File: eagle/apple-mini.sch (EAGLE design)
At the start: 30 parts, among them J1 USBMICRO, J2 RBM22DRTN, J3 JTAG, U1 FT240XS, U2 SN74LVC2G17DBV, U3 TPS2082D, U4 XC9572XL-10VQ64

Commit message: Add MPU and PIA to schematic
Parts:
- added C12, C13, C14, C15: 0.1uF, rcl:C-USC0805
- added R10, R11, R12: 100k, rcl:R-US_R0805
- added U5: 6821, apple-mini:6821
- added U6: 62256, apple-mini:62256
- added U7: 28C64, apple-mini:28C64
- added U8: XC9572XL-10VQ64, apple-mini:XC9572XL-10VQ64
- J2: value RBM22DRTN -> JTAG; device apple-mini:RBM22DRTN -> apple-mini:JTAG
- J3: value JTAG -> RBM22DRTN; device apple-mini:JTAG -> apple-mini:RBM22DRTN
- U2: value SN74LVC2G17DBV -> 74LVC2G17DBV; device apple-mini:SN74LVC2G17DBV -> apple-mini:74LVC2G17DBV
- U4: value XC9572XL-10VQ64 -> 6502; device apple-mini:XC9572XL-10VQ64 -> apple-mini:6502
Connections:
- net 3V3: now also C12.1, C13.1, C14.1, C15.1, J2.VREF, R10.2, R11.2, R12.2, U4P.VCC, U5G$1.CS1, U5G$1.PA7, U5P.VCC, U6P.VCC, U7P.VCC, U8PA.VCC, U8PB.VCC, U8PC.VCC, U8PD.VCC; no longer J3.VREF, U4PA.VCC, U4PB.VCC, U4PC.VCC, U4PD.VCC
- net 5V: now also J3.22; no longer J2.22
- net A0: now also J3.W, U4G$1.A0, U5G$1.RS0, U6G$1.A0, U7G$1.A0, U8G$1.P57; no longer J2.W, U4G$1.P57
- net A1: now also J3.19, U4G$1.A1, U5G$1.RS1, U6G$1.A1, U7G$1.A1, U8G$1.P59; no longer J2.19, U4G$1.P59
- net A10: now also J3.R, U4G$1.A10, U6G$1.A10, U7G$1.A10; no longer J2.R
- net A11: now also J3.14, U4G$1.A11, U6G$1.A11, U7G$1.A11; no longer J2.14
- net A12: now also J3.P, U4G$1.A12, U6G$1.A12, U7G$1.A12; no longer J2.P
- net A13: now also J3.13, U4G$1.A13, U6G$1.A13; no longer J2.13
- net A14: now also J3.N, U4G$1.A14, U6G$1.A14; no longer J2.N
- net A15: now also J3.12, U4G$1.A15; no longer J2.12
- net A2: now also J3.V, U4G$1.A2, U6G$1.A2, U7G$1.A2, U8G$1.P50; no longer J2.V, U4G$1.P50
- net A3: now also J3.18, U4G$1.A3, U6G$1.A3, U7G$1.A3, U8G$1.P2/GTS2; no longer J2.18, U4G$1.P2/GTS2
- net A4: now also J3.U, U4G$1.A4, U5G$1.CS0, U6G$1.A4, U7G$1.A4; no longer J2.U
- net A5: now also J3.17, U4G$1.A5, U6G$1.A5, U7G$1.A5; no longer J2.17
- net A6: now also J3.T, U4G$1.A6, U6G$1.A6, U7G$1.A6; no longer J2.T
- net A7: now also J3.16, U4G$1.A7, U6G$1.A7, U7G$1.A7; no longer J2.16
- net A8: now also J3.S, U4G$1.A8, U6G$1.A8, U7G$1.A8; no longer J2.S
- net A9: now also J3.15, U4G$1.A9, U6G$1.A9, U7G$1.A9; no longer J2.15
- net CA1: now also U5G$1.CA1, U8G$1.P52; no longer U4G$1.P52
- net CA2: now also U5G$1.CA2, U8G$1.P56; no longer U4G$1.P56
- net CB1: now also U5G$1.CB1, U8G$1.P19; no longer U4G$1.P19
- net CB2: now also U5G$1.CB2, U8G$1.P40; no longer U4G$1.P40
- net CLEAR: now also U8G$1.P31; no longer U4G$1.P31
- net CLK12MHZ: now also U8G$1.P16/GCK2; no longer U4G$1.P16/GCK2
- net D0: now also J3.9, U4G$1.D0, U5G$1.D0, U6G$1.D0, U7G$1.D0; no longer J2.9
- net D1: now also J3.J, U4G$1.D1, U5G$1.D1, U6G$1.D1, U7G$1.D1; no longer J2.J
- net D2: now also J3.8, U4G$1.D2, U5G$1.D2, U6G$1.D2, U7G$1.D2; no longer J2.8
- net D3: now also J3.H, U4G$1.D3, U5G$1.D3, U6G$1.D3, U7G$1.D3; no longer J2.H
- net D4: now also J3.7, U4G$1.D4, U5G$1.D4, U6G$1.D4, U7G$1.D4; no longer J2.7
- net D5: now also J3.F, U4G$1.D5, U5G$1.D5, U6G$1.D5, U7G$1.D5; no longer J2.F
- net D6: now also J3.6, U4G$1.D6, U5G$1.D6, U6G$1.D6, U7G$1.D6; no longer J2.6
- net D7: now also J3.E, U4G$1.D7, U5G$1.D7, U6G$1.D7, U7G$1.D7; no longer J2.E
- net DA: now also U5G$1.PB7, U8G$1.P20; no longer U4G$1.P20
- net FIFO_DATA0: now also U8G$1.P43; no longer U4G$1.P43
- net FIFO_DATA1: now also U8G$1.P44; no longer U4G$1.P44
- net FIFO_DATA2: now also U8G$1.P49; no longer U4G$1.P49
- net FIFO_DATA3: now also U8G$1.P51; no longer U4G$1.P51
- net FIFO_DATA4: now also U8G$1.P8; no longer U4G$1.P8
- net FIFO_DATA5: now also U8G$1.P9; no longer U4G$1.P9
- net FIFO_DATA6: now also U8G$1.P10; no longer U4G$1.P10
- net FIFO_DATA7: now also U8G$1.P39; no longer U4G$1.P39
- net FIFO_RD: now also U8G$1.P22; no longer U4G$1.P22
- net FIFO_RXF: now also U8G$1.P48; no longer U4G$1.P48
- net FIFO_TXE: now also U8G$1.P45; no longer U4G$1.P45
- net FIFO_WR: now also U8G$1.P18; no longer U4G$1.P18
- net GND: now also C12.2, C13.2, C14.2, C15.2, J2.GND, J3.20, J3.X, U4G$1.!SO, U4P.GND, U5P.GND, U6P.GND, U7P.GND, U8G$1.P15/GCK1, U8G$1.P17/GCK3, U8G$1.P23, U8G$1.P25, U8G$1.P32, U8G$1.P36, U8PA.GND, U8PB.GND, U8PC.GND, U8PD.GND; no longer J2.20, J2.X, J3.GND, U4G$1.P15/GCK1, U4G$1.P17/GCK3, U4G$1.P23, U4G$1.P25, U4G$1.P32, U4G$1.P36, U4PA.GND, U4PB.GND, U4PC.GND, U4PD.GND
- net IRQ: now also J3.4, R11.1, U4G$1.!IRQ; no longer J2.4
- net NMI: now also J3.3, R12.1, U4G$1.!NMI; no longer J2.3
- net PA0: now also U5G$1.PA0, U8G$1.P6; no longer U4G$1.P6
- net PA1: now also U5G$1.PA1, U8G$1.P60; no longer U4G$1.P60
- net PA2: now also U5G$1.PA2, U8G$1.P58; no longer U4G$1.P58
- net PA3: now also U5G$1.PA3, U8G$1.P62; no longer U4G$1.P62
- net PA4: now also U5G$1.PA4, U8G$1.P63; no longer U4G$1.P63
- net PA5: now also U5G$1.PA5, U8G$1.GSR/P64; no longer U4G$1.GSR/P64
- net PA6: now also U5G$1.PA6, U8G$1.P4; no longer U4G$1.P4
- net PB0: now also U5G$1.PB0, U8G$1.P61; no longer U4G$1.P61
- net PB1: now also U5G$1.PB1, U8G$1.P5/GTS1; no longer U4G$1.P5/GTS1
- net PB2: now also U5G$1.PB2, U8G$1.P46; no longer U4G$1.P46
- net PB3: now also U5G$1.PB3, U8G$1.P7; no longer U4G$1.P7
- net PB4: now also U5G$1.PB4, U8G$1.P11; no longer U4G$1.P11
- net PB5: now also U5G$1.PB5, U8G$1.P13; no longer U4G$1.P13
- net PB6: now also U5G$1.PB6, U8G$1.P12; no longer U4G$1.P12
- net PHI0: now also J3.M, U4G$1.PHI0, U8G$1.P24; no longer J2.M, U4G$1.P24
- net PHI1: now also J3.D, U4G$1.PHI1; no longer J2.D
- net PHI2: now also J3.A, U4G$1.PHI2, U5G$1.E, U8G$1.P47; no longer J2.A, U4G$1.P47
- net R: now also J3.L, U8G$1.P27; no longer J2.L, U4G$1.P27
- net RDY: now also J3.5, R10.1, U4G$1.RDY; no longer J2.5
- net RESET: now also J3.2, U4G$1.!RES, U5G$1.!RESET, U8G$1.P1; no longer J2.2, U4G$1.P1
- net RW: now also J3.K, U4G$1.R/!W, U5G$1.R/!W, U6G$1.!WE, U7G$1.!WE; no longer J2.K
- net S: now also J3.11, U8G$1.P33; no longer J2.11, U4G$1.P33
- net SYNC: now also J3.B, U4G$1.SYNC; no longer J2.B
- net T: now also J3.21, U8G$1.P35; no longer J2.21, U4G$1.P35
- net TCK: now also J2.TCK, U8G$1.TCK; no longer J3.TCK, U4G$1.TCK
- net TDI: now also J2.TDI, U8G$1.TDI; no longer J3.TDI, U4G$1.TDI
- net TDO: now also J2.TDO, U8G$1.TDO; no longer J3.TDO, U4G$1.TDO
- net TMS: now also J2.TMS, U8G$1.TMS; no longer J3.TMS, U4G$1.TMS
- net X: now also U6G$1.!CE, U6G$1.!OE, U8G$1.P34; no longer U4G$1.P34
- net Y: now also U7G$1.!CE, U7G$1.!OE, U8G$1.P42; no longer U4G$1.P42
- net Z: now also U5G$1.!CS2, U8G$1.P38; no longer U4G$1.P38
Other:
- note added: "MEMORY MAP X 0000 7FFF RAM T A000 AFFF S B000 BFFF R C000 CFFF Z D000 DFFF PIA Y E000 FFFF EEPROM"

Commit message: Finalize schematic; initial board placement
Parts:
- C1, C10, C11, C12, C13, C14, C15, C2, C3, C6, C7, C8, C9: device rcl:C-USC0805 -> apple-mini:C0603
- C4, C5: value 0.22uF -> 2.2uF; device rcl:C-USC0805 -> apple-mini:C0603
- D1: value (none) -> CHIPLED; device led:LEDCHIP-LED0805 -> apple-mini:CHIPLED
- R1, R2: device rcl:R-US_R0805 -> apple-mini:R0402
- R10, R11, R12, R4, R5: value 100k -> 10k; device rcl:R-US_R0805 -> apple-mini:R0603
- R3, R9: value 100k -> 4.7k; device rcl:R-US_R0805 -> apple-mini:R0603
- R6, R7, R8: device rcl:R-US_R0805 -> apple-mini:R0603
- U2: value 74LVC2G17DBV -> SN74LVC2G17DBV; device apple-mini:74LVC2G17DBV -> apple-mini:SN74LVC2G17DBV
- U4: value 6502 -> MCS6502; device apple-mini:6502 -> apple-mini:MCS6502
- U5: value 6821 -> MC6821; device apple-mini:6821 -> apple-mini:MC6821
- U6: value 62256 -> AS6C62256A; device apple-mini:62256 -> apple-mini:AS6C62256A
- U7: value 28C64 -> AT28C64B; device apple-mini:28C64 -> apple-mini:AT28C64B
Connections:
- net 3V3: no longer C10.1, C11.1, C2.1, C8.1, C9.1, R10.2, R11.2, R12.2, R4.2, R5.2, U2P.VCC, U4P.VCC, U5G$1.CS1, U5G$1.PA7, U5P.VCC, U6P.VCC, U7P.VCC
- net 5V: now also C10.1, C11.1, C2.1, C8.1, C9.1, D1.2, R10.2, R11.2, R12.2, R4.2, R5.2, U2P.VCC, U4P.VCC, U5G$1.CS1, U5G$1.PA7, U5P.VCC, U6P.VCC, U7P.VCC; no longer D1.A
- net CLEAR: now also U2B.Y; no longer U2A.Y
- net GND: now also RESET.3; no longer RESET.4
- net N$1: now also D1.1; no longer D1.C
- net N$2: now also R7.1; no longer R6.1
- net N$3: now also R6.1, RESET.1; no longer R7.1, RESET.2
- net RESET: now also U2A.Y, U4G$1.!RESET; no longer U2B.Y, U4G$1.!RES
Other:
- note added: "KEYBOARD"
- note added: "TERMINAL"
- moved on the sheet: C1, C10, C11, C12, C13, C14, C15, C2, C4, C5, C8, C9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

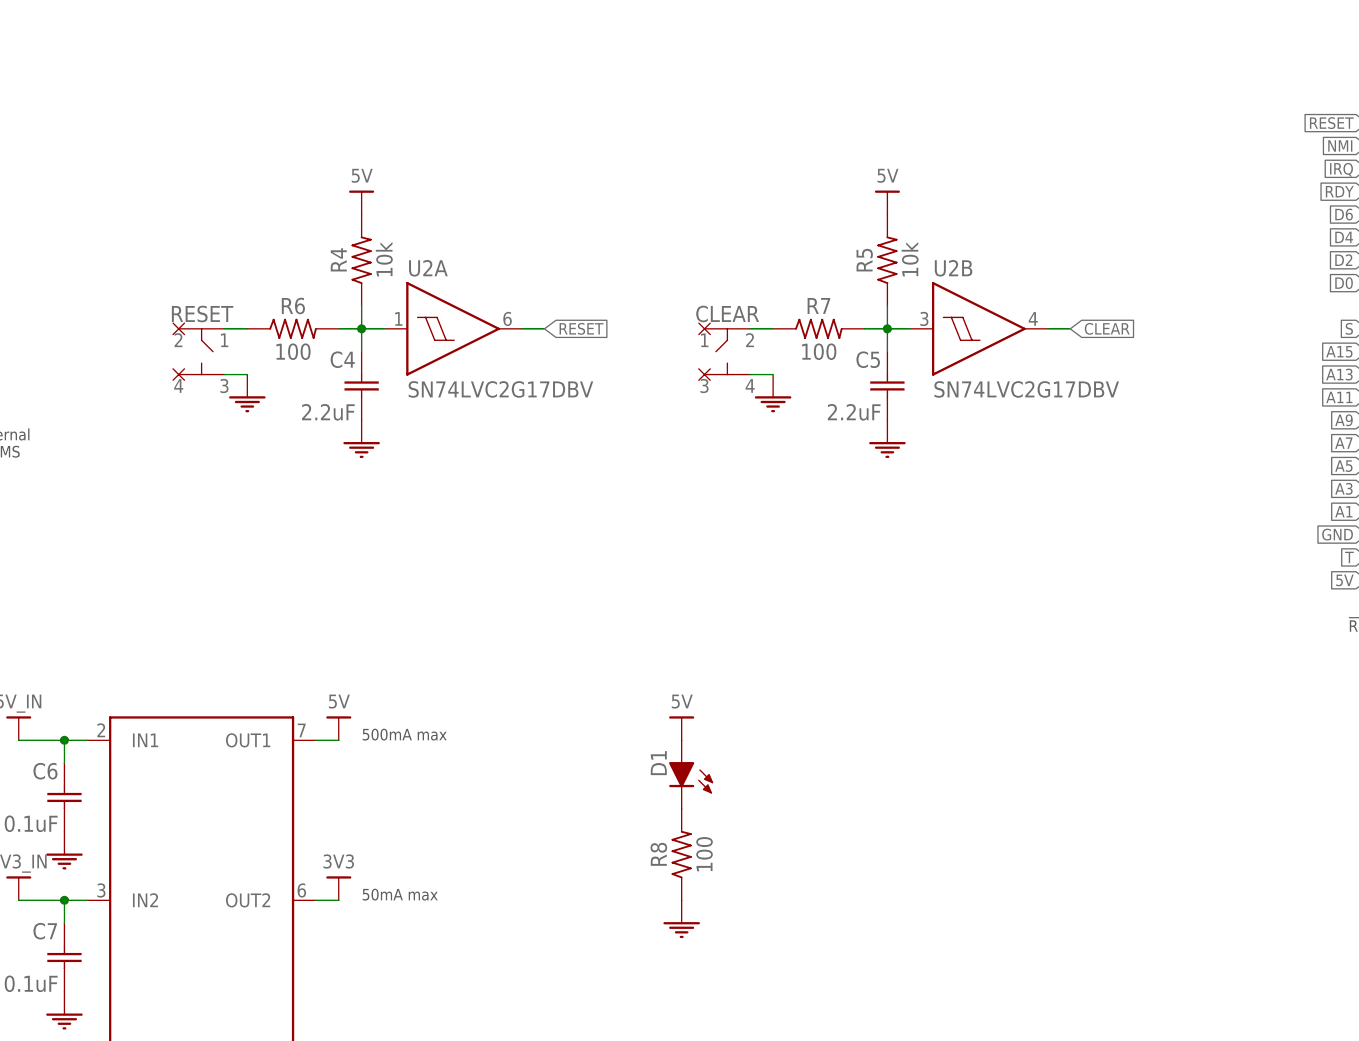
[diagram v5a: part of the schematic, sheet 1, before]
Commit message: Add DRC rules and logo bitmap to board layout
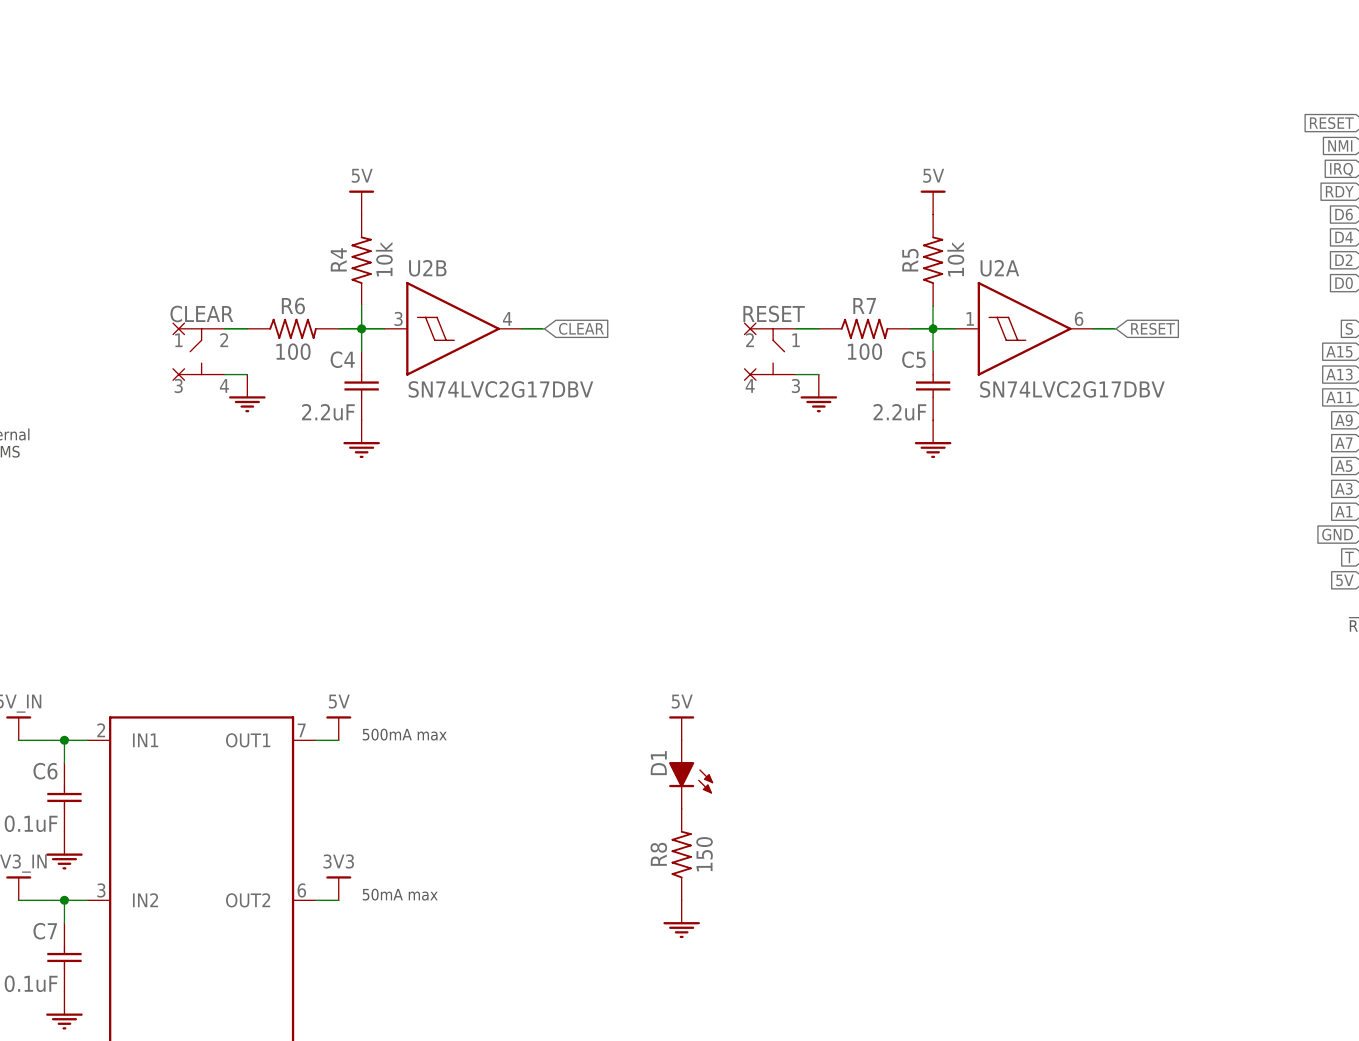
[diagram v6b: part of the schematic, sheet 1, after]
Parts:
- R8: value 100 -> 150
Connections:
- net N$2: now also R6.1; no longer R7.1
- net N$3: now also R7.1; no longer R6.1
- net N$4: now also C4.1, R4.1, R6.2; no longer C5.1, R5.1, R7.2
- net N$5: now also C5.1, R5.1, R7.2; no longer C4.1, R4.1, R6.2
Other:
- moved on the sheet: C5, CLEAR, R5, R7, RESET, U2A, U2B

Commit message: Generate BOM
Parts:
- C1, C10, C11, C12, C13, C14, C15, C2, C3, C6, C7, C8, C9: COMMENTS (none) -> 16V 10% X7R MLCC; MFR (none) -> Kemet; MFR_PARTNO (none) -> C0603C104K4RACTU; VENDOR (none) -> Digi-Key; VENDOR_PARTNO (none) -> 399-1096-1-ND
- C4, C5: value 2.2uF -> 0.22uF; COMMENTS (none) -> 16V 10% X7R MLCC; MFR (none) -> TDK; MFR_PARTNO (none) -> C1608X7R1C224K080AC; VENDOR (none) -> Digi-Key; VENDOR_PARTNO (none) -> 445-1318-1-ND
- CLEAR, RESET: VENDOR (none) -> Digi-Key; VENDOR_PARTNO (none) -> CKN9088CT-ND
- D1: COMMENTS (none) -> 2V 20mA; MFR (none) -> Lite-On; MFR_PARTNO (none) -> LTST-C190KGKT; VENDOR (none) -> Digi-Key; VENDOR_PARTNO (none) -> 160-1435-1-ND
- J1: VENDOR (none) -> Digi-Key; VENDOR_PARTNO (none) -> 609-4616-1-ND
- J2: VENDOR (none) -> Digi-Key; VENDOR_PARTNO (none) -> WM18641-ND
- J3: VENDOR (none) -> Digi-Key; VENDOR_PARTNO (none) -> RBM22DRTN-ND
- R1, R2: COMMENTS (none) -> 5% 1/16W; MFR (none) -> Yageo; MFR_PARTNO (none) -> RC0402JR-0727RL; VENDOR (none) -> Digi-Key; VENDOR_PARTNO (none) -> 311-27JRCT-ND
- R10, R11, R12: COMMENTS (none) -> 5% 1/10W; MFR (none) -> Yageo; MFR_PARTNO (none) -> RC0603JR-0710KL; VENDOR (none) -> Digi-Key; VENDOR_PARTNO (none) -> 311-10KGRCT-ND
- R3, R9: COMMENTS (none) -> 5% 1/10W; MFR (none) -> Yageo; MFR_PARTNO (none) -> RC0603JR-074K7L; VENDOR (none) -> Digi-Key; VENDOR_PARTNO (none) -> 311-4.7KGRCT-ND
- R4, R5: value 10k -> 100k; COMMENTS (none) -> 5% 1/10W; MFR (none) -> Yageo; MFR_PARTNO (none) -> RC0603JR-07100KL; VENDOR (none) -> Digi-Key; VENDOR_PARTNO (none) -> 311-100KGRCT-ND
- R6, R7: COMMENTS (none) -> 5% 1/4W; MFR (none) -> Rohm Semiconductor; MFR_PARTNO (none) -> ESR03EZPJ101; VENDOR (none) -> Digi-Key; VENDOR_PARTNO (none) -> RHM100DCT-ND
- R8: value 150 -> 180; COMMENTS (none) -> 5% 1/4W; MFR (none) -> Rohm Semiconductor; MFR_PARTNO (none) -> ESR03EZPJ181; VENDOR (none) -> Digi-Key; VENDOR_PARTNO (none) -> RHM180DCT-ND
- U1: VENDOR (none) -> Digi-Key; VENDOR_PARTNO (none) -> 768-1158-5-ND
- U2: VENDOR (none) -> Digi-Key; VENDOR_PARTNO (none) -> 296-13012-1-ND
- U3: VENDOR (none) -> Digi-Key; VENDOR_PARTNO (none) -> 296-3433-5-ND
- U4: VENDOR (none) -> Jameco; VENDOR_PARTNO (none) -> 43191
- U5: VENDOR (none) -> Jameco; VENDOR_PARTNO (none) -> 43596
- U6: VENDOR (none) -> Digi-Key; VENDOR_PARTNO (none) -> 1450-1182-5-ND
- U7: VENDOR (none) -> Digi-Key; VENDOR_PARTNO (none) -> AT28C64B-15PU-ND
- U8: VENDOR (none) -> Digi-Key; VENDOR_PARTNO (none) -> 122-1388-ND
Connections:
- net GND: now also CLEAR.2; no longer CLEAR.4, RESET.3
- net N$2: now also CLEAR.1; no longer CLEAR.2
- net N$3: no longer RESET.1

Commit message: Route critical signals
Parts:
- C4, C5: value 0.22uF -> 2.2uF; COMMENTS 16V 10% X7R MLCC -> 16V 10% X5R MLCC; MFR TDK -> Kemet; MFR_PARTNO C1608X7R1C224K080AC -> C0603C225K4PACTU; VENDOR_PARTNO 445-1318-1-ND -> 399-7886-1-ND
- CLEAR, RESET: COMMENTS (none) -> 12V 50mA
- D1: COMMENTS 2V 20mA -> 2.0-2.5V 20mA
- R4, R5: value 100k -> 10k; MFR_PARTNO RC0603JR-07100KL -> RC0603JR-0710KL; VENDOR_PARTNO 311-100KGRCT-ND -> 311-10KGRCT-ND
- R8: value 180 -> 150
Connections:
- net N$3_P renamed N$1_P
- net N$4_P renamed N$2_P
- net A0: no longer U8G$1.P57
- net A1: no longer U8G$1.P59
- net A12: now also U8G$1.P33
- net A13: now also U8G$1.P34
- net A14: now also U8G$1.P35
- net A15: now also U8G$1.P36
- net A2: no longer U8G$1.P50
- net A3: no longer U8G$1.P2/GTS2
- net CA1: now also U8G$1.P61; no longer U8G$1.P52
- net CA2: now also U8G$1.P62; no longer U8G$1.P56
- net CB1: now also U8G$1.P63; no longer U8G$1.P19
- net CB2: now also U8G$1.GSR/P64; no longer U8G$1.P40
- net CLEAR: now also U8G$1.P49; no longer U8G$1.P31
- net DA: now also U8G$1.P47; no longer U8G$1.P20
- net FIFO_DATA0: now also U8G$1.P1; no longer U8G$1.P43
- net FIFO_DATA1: now also U8G$1.P2/GTS2; no longer U8G$1.P44
- net FIFO_DATA2: now also U8G$1.P4; no longer U8G$1.P49
- net FIFO_DATA3: now also U8G$1.P5/GTS1; no longer U8G$1.P51
- net FIFO_DATA4: now also U8G$1.P6; no longer U8G$1.P8
- net FIFO_DATA5: now also U8G$1.P7; no longer U8G$1.P9
- net FIFO_DATA6: now also U8G$1.P8; no longer U8G$1.P10
- net FIFO_DATA7: now also U8G$1.P9; no longer U8G$1.P39
- net FIFO_RD: now also U8G$1.P10; no longer U8G$1.P22
- net FIFO_RXF: now also U8G$1.P12; no longer U8G$1.P48
- net FIFO_TXE: now also U8G$1.P13; no longer U8G$1.P45
- net FIFO_WR: now also U8G$1.P11; no longer U8G$1.P18
- net GND: now also RESET.2, U8G$1.P18, U8G$1.P27, U8G$1.P31, U8G$1.P38, U8G$1.P50; no longer U8G$1.P17/GCK3, U8G$1.P23, U8G$1.P25, U8G$1.P32, U8G$1.P36
- net N$3: now also RESET.1
- net PA0: now also U8G$1.P51; no longer U8G$1.P6
- net PA1: now also U8G$1.P52; no longer U8G$1.P60
- net PA2: now also U8G$1.P56; no longer U8G$1.P58
- net PA3: now also U8G$1.P57; no longer U8G$1.P62
- net PA4: now also U8G$1.P58; no longer U8G$1.P63
- net PA5: now also U8G$1.P59; no longer U8G$1.GSR/P64
- net PA6: now also U8G$1.P60; no longer U8G$1.P4
- net PB0: now also U8G$1.P39; no longer U8G$1.P61
- net PB1: now also U8G$1.P40; no longer U8G$1.P5/GTS1
- net PB2: now also U8G$1.P42; no longer U8G$1.P46
- net PB3: now also U8G$1.P43; no longer U8G$1.P7
- net PB4: now also U8G$1.P44; no longer U8G$1.P11
- net PB5: now also U8G$1.P45; no longer U8G$1.P13
- net PB6: now also U8G$1.P46; no longer U8G$1.P12
- net PHI0: now also U8G$1.P17/GCK3; no longer U8G$1.P24
- net PHI2: now also U8G$1.P32; no longer U8G$1.P47
- net R: now also U8G$1.P19; no longer U8G$1.P27
- net RESET: now also U8G$1.P48; no longer U8G$1.P1
- net S: now also U8G$1.P20; no longer U8G$1.P33
- net T: now also U8G$1.P22; no longer U8G$1.P35
- net X: now also U8G$1.P23; no longer U8G$1.P34
- net Y: now also U8G$1.P24; no longer U8G$1.P42
- net Z: now also U8G$1.P25; no longer U8G$1.P38
